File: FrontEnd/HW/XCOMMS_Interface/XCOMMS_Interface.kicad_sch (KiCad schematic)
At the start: 17 parts

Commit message: Altium to KiCad translation of interface board
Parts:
- removed C?: Cap Semi, 0805 SMD Capacitor, symbol COMMS2-altium-import:1_Cap Semi
- removed C? (x4): Cap Semi, 0603 SMD Capacitor, symbol COMMS2-altium-import:3_Cap Semi
- removed C?: Cap Semi, 0603 SMD Capacitor, symbol COMMS2-altium-import:1_Cap Semi
- removed R?: Res3, 0603 SMD Resistor, symbol COMMS2-altium-import:0_Res3
- removed SCRW? (x4): Metric Screw Hole, M3 ScrewHole, symbol COMMS2-altium-import:0_ScrewHole
- removed U?: STM32L4, QFN-33N, symbol COMMS2-altium-import:0_STM32L431Kx
- removed Y?: TCXO 10 MHz, ECS-TXO-2016, symbol COMMS2-altium-import:0_ECS-TXO-2016
- added C1: 4.7uF, Capacitor_SMD:C_0805_2012Metric, symbol Device:C
- added C2, C5: 1uF, Capacitor_SMD:C_0603_1608Metric, symbol Device:C
- added C3, C4, C6: 100nF, Capacitor_SMD:C_0603_1608Metric, symbol Device:C
- added R1: 510, Resistor_SMD:R_0603_1608Metric, symbol Device:R
- added SCRW1, SCRW2, SCRW3, SCRW4: MountingHole_Pad, MountingHole:MountingHole_3.2mm_M3_Pad_Via, symbol Mechanical:MountingHole_Pad
- added U1: STM32L431KBUx, Package_DFN_QFN:QFN-32-1EP_5x5mm_P0.5mm_EP3.45x3.45mm, symbol MCU_ST_STM32L4:STM32L431KBUx
- added Y1: TCXO_ECS, GGS_Miscellaneous:TCXO_ECS, symbol GGS_Miscellaneous:TCXO_ECS
- 12V1: renamed from 12 V?; footprint 532610271 -> Connector_Molex:Molex_PicoBlade_53261-0271_1x02-1MP_P1.25mm_Horizontal; symbol COMMS2-altium-import:0_MOLEX_532610271 -> GGS_Connectors:Picoblade_2x1_H
- JTAG1: renamed from JTAG?; value 532610471 -> MOLEX_532610471; footprint 532610471 -> Connector_Molex:Molex_PicoBlade_53261-0471_1x04-1MP_P1.25mm_Horizontal; symbol COMMS2-altium-import:0_MOLEX_532610471 -> GGS_Connectors:Picoblade_4x1_H
- UART1: renamed from UART?; value 532610471 -> MOLEX_532610471; footprint 532610471 -> Connector_Molex:Molex_PicoBlade_53261-0471_1x04-1MP_P1.25mm_Horizontal; symbol COMMS2-altium-import:0_MOLEX_532610471 -> GGS_Connectors:Picoblade_4x1_H
- gave numbers to parts that had none: 1
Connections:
- net 3V3: now also J1.02; no longer J1.2
- net 5V: now also J1.01; no longer J1.1
- net 5V_EN: now also U1.15 (PB1)
- net 6V_EN: now also U1.14 (PB0)
- net CurrentSense: now also U1.8 (PA2)
- net GND: now also 12V1.MP (MH2), J1.06, J1.08, JTAG1.MP (MH2), UART1.MP (MH2), C1.2, C2.2, C3.2, C4.2, C5.2, C6.2, R1.2, SCRW1.1, SCRW2.1, SCRW3.1, SCRW4.1, U1.16 (VSS), U1.32 (VSS), U1.33 (VSS), Y1.2 (GND); no longer 12V1.0 (MH2), J1.6, J1.8, JTAG1.0 (MH2), UART1.0 (MH2)
- net JTCK: now also U1.24 (PA14)
- net JTDI: now also U1.25 (PA15)
- net JTDO: now also U1.26 (PB3)
- net JTMS: now also U1.23 (PA13)
- net LO_EN: now also J1.05, U1.10 (PA4); no longer J1.5
- net PLL_CSB: now also U1.28 (PB5)
- net R_CSB: now also U1.29 (PB6)
- net SCK: now also U1.11 (PA5)
- net SDI: now also U1.13 (PA7)
- net SDO: now also U1.12 (PA6)
- net T_CSB: now also J1.07, U1.30 (PB7); no longer J1.7
- net Tx_CE: now also J1.09, U1.27 (PB4); no longer J1.9
- net Tx_PM: now also J1.04, U1.7 (PA1); no longer J1.4
- net USART1_CTS: now also U1.21 (PA11)
- net USART1_Rx: now also U1.20 (PA10)
- net USART1_Tx: now also U1.19 (PA9)
- net Vd_PA: now also J1.03; no longer J1.3
- net mcu_OSC: now also U1.6 (PA0), Y1.3 (Out)
- net 12V renamed +12V
- new net +3V3: C1.1, C2.1, C3.1, C4.1, C5.1, C6.1, U1.1 (VDD), U1.17 (VDD), U1.5 (VDDA), Y1.1 (TriState), Y1.4 (Vdd)
- new net Boot0: R1.1, U1.31 (PH3)
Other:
- sheet XCOMMS_PowerSupply ports: added 12V, 3V3, 5V, 5V_EN, 6V_EN, CurrentSense, R_CSB, SCK, SDI, Vd_PA, Vg_PA1, Vg_PA2, Vg_PA3, gnd; removed none
- note added: "Connectors"
- note added: "MCU"
- note added: "Power Supply"
- note added: "Screws"
- note added: "falta cout"
- note removed: "GND has to be connected to JTAG"
- note removed: "nRST has to be connected with JTAG"
- moved on the sheet: 12V1, J1, JTAG1, UART1

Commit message: XCOMMS_RF and XCOMMS_Interface KiCad design updated
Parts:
- added C_TCXO1: 100nF, Capacitor_SMD:C_0603_1608Metric, symbol Device:C
- J2: renamed from UART1; value MOLEX_532610471 -> UART
- J3: renamed from JTAG1; value MOLEX_532610471 -> JTAG
- J4: renamed from 12V1; value MOLEX_52610271 -> 12V
- R1: value 510 -> 10k
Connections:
- net GND: now also C_TCXO1.2
- net mcu_OSC: now also C_TCXO1.1
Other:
- note removed: "falta cout"
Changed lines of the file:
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@@
-    (effects (font (size 1.27 1.27)) (justify left bottom))
-  )
-  (text "falta cout" (at 86.36 82.55 0)
     (effects (font (size 1.27 1.27)) (justify left bottom))
   )
@@
   (symbol (lib_id "GGS_Connectors:Picoblade_4x1_H") (at 97.79 154.94 0) (unit 1)
     (in_bom yes) (on_board yes) (fields_autoplaced)
-    (property "Reference" "JTAG1" (id 0) (at 96.52 134.62 0))
-    (property "Value" "MOLEX_532610471" (id 1) (at 96.52 137.16 0))
+    (property "Reference" "J3" (id 0) (at 96.52 134.62 0))
+    (property "Value" "JTAG" (id 1) (at 96.52 137.16 0))
     (property "Footprint" "Connector_Molex:Molex_PicoBlade_53261-0471_1x04-1MP_P1.25mm_Horizontal" (id 2) (at 97.79 154.94 0)
       (effects (font (size 1.27 1.27)) hide)
@@
     )
     (pin "1")
+  )
+  (symbol (lib_id "Device:C") (at 88.9 82.55 0) (unit 1)
+    (in_bom yes) (on_board yes) (fields_autoplaced)
+    (property "Reference" "C_TCXO1" (id 0) (at 92.71 81.2799 0)
+      (effects (font (size 1.27 1.27)) (justify left))
+    )
+    (property "Value" "100nF" (id 1) (at 92.71 83.8199 0)
+      (effects (font (size 1.27 1.27)) (justify left))
+    )
+    (property "Footprint" "Capacitor_SMD:C_0603_1608Metric" (id 2) (at 89.8652 86.36 0)
+      (effects (font (size 1.27 1.27)) hide)
+    )
+    (property "Datasheet" "~" (id 3) (at 88.9 82.55 0)
+      (effects (font (size 1.27 1.27)) hide)
+    )
+    (pin "1")
+    (pin "2")
   )
   (symbol (lib_id "MCU_ST_STM32L4:STM32L431KBUx") (at 124.46 68.58 0) (unit 1)
@@
   (symbol (lib_id "GGS_Connectors:Picoblade_2x1_H") (at 132.08 154.94 0) (unit 1)
     (in_bom yes) (on_board yes) (fields_autoplaced)
-    (property "Reference" "12V1" (id 0) (at 132.08 139.7 0))
-    (property "Value" "MOLEX_52610271" (id 1) (at 132.08 142.24 0))
+    (property "Reference" "J4" (id 0) (at 132.08 139.7 0))
+    (property "Value" "12V" (id 1) (at 132.08 142.24 0))
     (property "Footprint" "Connector_Molex:Molex_PicoBlade_53261-0271_1x02-1MP_P1.25mm_Horizontal" (id 2) (at 132.08 154.94 0)
       (effects (font (size 1.27 1.27)) hide)
@@
     (pin "1")
   )
+  (symbol (lib_id "power:GND") (at 88.9 86.36 0) (unit 1)
+    (in_bom yes) (on_board yes) (fields_autoplaced)
+    (property "Reference" "#PWR0101" (id 0) (at 88.9 92.71 0)
+      (effects (font (size 1.27 1.27)) hide)
+    )
+    (property "Value" "GND" (id 1) (at 88.9 91.44 0))
+    (property "Footprint" "" (id 2) (at 88.9 86.36 0)
+      (effects (font (size 1.27 1.27)) hide)
+    )
+    (property "Datasheet" "" (id 3) (at 88.9 86.36 0)
+      (effects (font (size 1.27 1.27)) hide)
+    )
+    (pin "1")
+  )
   (symbol (lib_id "power:+3V3") (at 44.5118 71.12 0) (unit 1)
     (in_bom yes) (on_board yes) (fields_autoplaced)
@@
       (effects (font (size 1.27 1.27)) (justify left))
     )
-    (property "Value" "510" (id 1) (at 101.6 66.0399 0)
+    (property "Value" "10k" (id 1) (at 101.6 66.0399 0)
       (effects (font (size 1.27 1.27)) (justify left))
     )
@@
   (symbol (lib_id "GGS_Connectors:Picoblade_4x1_H") (at 97.79 134.62 0) (unit 1)
     (in_bom yes) (on_board yes) (fields_autoplaced)
-    (property "Reference" "UART1" (id 0) (at 96.52 114.3 0))
-    (property "Value" "MOLEX_532610471" (id 1) (at 96.52 116.84 0))
+    (property "Reference" "J2" (id 0) (at 96.52 114.3 0))
+    (property "Value" "UART" (id 1) (at 96.52 116.84 0))
     (property "Footprint" "Connector_Molex:Molex_PicoBlade_53261-0471_1x04-1MP_P1.25mm_Horizontal" (id 2) (at 97.79 134.62 0)
       (effects (font (size 1.27 1.27)) hide)
@@
       (reference "#PWR072") (unit 1) (value "GND") (footprint "")
     )
-    (path "/7af7be37-6e93-4ed7-bb28-3b6dfcb278ed"
-      (reference "12V1") (unit 1) (value "MOLEX_52610271") (footprint "Connector_Molex:Molex_PicoBlade_53261-0271_1x02-1MP_P1.25mm_Horizontal")
+    (path "/8e8c5498-761b-4fad-8a9e-870d060ec873"
+      (reference "#PWR0101") (unit 1) (value "GND") (footprint "")
     )
     (path "/2f6555cb-8bb3-48ae-8adc-4aebbd8da0ca"
@@
       (reference "C40") (unit 1) (value "0.33uF") (footprint "Capacitor_SMD:C_0603_1608Metric")
     )
+    (path "/657fa770-7c96-4254-95e9-81a8281c58b4"
+      (reference "C_TCXO1") (unit 1) (value "100nF") (footprint "Capacitor_SMD:C_0603_1608Metric")
+    )
     (path "/0c671ed6-a6a6-4798-a2b6-204ff4387a8c"
       (reference "J1") (unit 1) (value "TFC-110-02-F-D-A-P-FR") (footprint "GGS_Connectors:SAMTEC_TFC-110-02-F-D-A-P-FR")
     )
+    (path "/b50c6642-ec2d-4f21-8bcb-af36206e84ce"
+      (reference "J2") (unit 1) (value "UART") (footprint "Connector_Molex:Molex_PicoBlade_53261-0471_1x04-1MP_P1.25mm_Horizontal")
+    )
     (path "/0f9289a9-c07b-4423-9227-e6c4d7d06c30"
-      (reference "JTAG1") (unit 1) (value "MOLEX_532610471") (footprint "Connector_Molex:Molex_PicoBlade_53261-0471_1x04-1MP_P1.25mm_Horizontal")
+      (reference "J3") (unit 1) (value "JTAG") (footprint "Connector_Molex:Molex_PicoBlade_53261-0471_1x04-1MP_P1.25mm_Horizontal")
+    )
+    (path "/7af7be37-6e93-4ed7-bb28-3b6dfcb278ed"
+      (reference "J4") (unit 1) (value "12V") (footprint "Connector_Molex:Molex_PicoBlade_53261-0271_1x02-1MP_P1.25mm_Horizontal")
     )
     (path "/1c391ca7-e610-404c-bdff-cd84da814875/575f37ba-97c6-45e5-8a2e-5226df8b97ca"
@@
     )
     (path "/b0dc419d-1860-444a-995b-e370e75d4f19"
-      (reference "R1") (unit 1) (value "510") (footprint "Resistor_SMD:R_0603_1608Metric")
+      (reference "R1") (unit 1) (value "10k") (footprint "Resistor_SMD:R_0603_1608Metric")
     )
     (path "/1c391ca7-e610-404c-bdff-cd84da814875/40b0f3e7-81f1-464f-ba85-11bb7be3476c"
@@
       (reference "U10") (unit 1) (value "MAX870EUK") (footprint "Package_TO_SOT_SMD:SOT-23-5")
     )
-    (path "/b50c6642-ec2d-4f21-8bcb-af36206e84ce"
-      (reference "UART1") (unit 1) (value "MOLEX_532610471") (footprint "Connector_Molex:Molex_PicoBlade_53261-0471_1x04-1MP_P1.25mm_Horizontal")
-    )
     (path "/0e2e05a9-b1d6-423e-ad08-77f5118bb25b"

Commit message: XCOMMS RF update and PA EvalBoard
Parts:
- SCRW1, SCRW2, SCRW3, SCRW4: footprint MountingHole:MountingHole_3.2mm_M3_Pad_Via -> MountingHole:MountingHole_2.7mm_M2.5_Pad
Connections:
- net USART1_CK is gone; now on net GND: J2.4
- net +12V: now also J4.1; no longer J4.2
- net GND: now also J4.2; no longer J4.1
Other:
- note added: "19-03-2022"
- note added: "To Do: Reduce voltage gate inverters to 1 Add LDO for PA Change Picoblade locations"
- note added: "XCOMMS_Interface_v2"
- moved on the sheet: C1, C2, C3, C4, C5, C6, C_TCXO1, J1, J2, J3, J4, R1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

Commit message: XCOMMS Interface rebuild
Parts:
- removed C_TCXO1: 100nF, Capacitor_SMD:C_0603_1608Metric, symbol Device:C
- removed J2: UART, Connector_Molex:Molex_PicoBlade_53261-0471_1x04-1MP_P1.25mm_Horizontal, symbol GGS_Connectors:Picoblade_4x1_H
- removed J3: JTAG, Connector_Molex:Molex_PicoBlade_53261-0471_1x04-1MP_P1.25mm_Horizontal, symbol GGS_Connectors:Picoblade_4x1_H
- removed J4: 12V, Connector_Molex:Molex_PicoBlade_53261-0271_1x02-1MP_P1.25mm_Horizontal, symbol GGS_Connectors:Picoblade_2x1_H
- removed U1: STM32L431KBUx, Package_DFN_QFN:QFN-32-1EP_5x5mm_P0.5mm_EP3.45x3.45mm, symbol MCU_ST_STM32L4:STM32L431KBUx
- removed Y1: TCXO_ECS, GGS_Miscellaneous:TCXO_ECS, symbol GGS_Miscellaneous:TCXO_ECS
- added Annotation1: Silkscreen_Annotation, GGS_Symbols:Bike, symbol GGS_Symbols:Silkscreen_Annotation
- added Annotation2: Silkscreen_Annotation, GGS_Symbols:GGS, symbol GGS_Symbols:Silkscreen_Annotation
- added Annotation3: Silkscreen_Annotation, GGS_Symbols:NSL, symbol GGS_Symbols:Silkscreen_Annotation
- added Annotation4: Silkscreen_Annotation, GGS_Symbols:Prj, symbol GGS_Symbols:Silkscreen_Annotation
- added Annotation5: Silkscreen_Annotation, GGS_Symbols:Rev, symbol GGS_Symbols:Silkscreen_Annotation
- added Annotation6: Silkscreen_Annotation, GGS_Symbols:UPC, symbol GGS_Symbols:Silkscreen_Annotation
- added C41: 20nF, Capacitor_SMD:C_0603_1608Metric, symbol Device:C
- added D1, D2, D3, D4, D5: SZESD9X3.3ST5G, Diode_SMD:D_SOD-923, symbol Device:D_TVS
- added J2, J3: PicoBlade01x05, Connector_Molex:Molex_PicoBlade_53261-0571_1x05-1MP_P1.25mm_Horizontal, symbol Connector_Generic_MountingPin:Conn_01x05_MountingPin
- added J4: PicoBlade01x02, Connector_Molex:Molex_PicoBlade_53261-0271_1x02-1MP_P1.25mm_Horizontal, symbol Connector_Generic_MountingPin:Conn_01x02_MountingPin
- added R22, R23, R24: 10k, Resistor_SMD:R_0603_1608Metric, symbol Device:R
- added R25, R26, R27, R28, R29: 22R, Resistor_SMD:R_0603_1608Metric, symbol Device:R
- added U1: STM32L051K8Tx, Package_QFP:LQFP-32_7x7mm_P0.8mm, symbol MCU_ST_STM32L0:STM32L051K8Tx
- added Y1: ECS-160-8-36B-CKY-TR3, Oscillator:Oscillator_SMD_ECS_2520MV-xxx-xx-4Pin_2.5x2.0mm, symbol Device:Crystal_GND24
- C1: footprint Capacitor_SMD:C_0805_2012Metric -> Capacitor_SMD:C_0603_1608Metric
- C5: value 1uF -> 100nF
- C6: value 100nF -> 20nF
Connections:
- net 3V3 is gone; now on net Vd_PA: J1.02
- net LO_EN is gone; now on net Vg_PA2: J1.05
- net +12V: now also J3.1 (Pin_1), J4.1 (Pin_1)
- net +3V3: now also J1.12, J2.1 (Pin_1), R22.1, R23.1, R24.1, U1.1 (VDD), U1.17 (VDD), U1.5 (VDDA); no longer C5.1, C6.1
- net 5V_EN: now also U1.15 (PB1)
- net 6V_EN: now also U1.14 (PB0)
- net GND: now also J1.09, J1.15, J1.17, J1.19, C41.2, D1.1 (A1), D2.1 (A1), D3.1 (A1), D4.1 (A1), D5.1 (A1), J2.2 (Pin_2), J2.MP (MountPin), J3.4 (Pin_4), J3.5 (Pin_5), J3.MP (MountPin), J4.2 (Pin_2), J4.MP (MountPin), U1.16 (VSS), U1.32 (VSS), Y1.2, Y1.4; no longer J1.08, J1.10, J1.12
- net PLL_CSB: now also U1.28 (PB5)
- net R_CSB: now also U1.9 (PA3)
- net SCK: now also J1.16, U1.11 (PA5); no longer J1.15
- net SDI: now also J1.20, U1.13 (PA7); no longer J1.19
- net SDO: now also J1.18, U1.12 (PA6); no longer J1.17
- net T_CSB: now also J1.08, U1.22 (PA12); no longer J1.07
- net Tx_CE: now also U1.27 (PB4); no longer J1.09
- net Vd_PA: no longer J1.03
- net Vg_PA1: now also J1.07; no longer J1.20
- net Vg_PA2: no longer J1.18
- net Vg_PA3: now also J1.03; no longer J1.16
- net 5V renamed Pout_PA
- net Pout_PA: now also U1.7 (PA1)
- net Boot0 renamed BOOT0
- net BOOT0: now also U1.31 (BOOT0)
- net Tx_PM renamed +5V
- new net: J2.3 (Pin_3), R25.2
- new net: J2.5 (Pin_5), R27.2
- new net: J3.2 (Pin_2), R28.2
- new net: J2.4 (Pin_4), R26.2
- new net: J3.3 (Pin_3), R29.2
- new net I2C1_SCL: D4.2 (A2), R24.2, R28.1, U1.29 (PB6)
- new net I2C1_SDA: D5.2 (A2), R23.2, R29.1, U1.30 (PB7)
- new net Id_PA: U1.8 (PA2)
- new net NRST: C5.1, D3.2 (A2), R22.2, R27.1, U1.4 (NRST)
- new net PLL_CE: J1.10
- new net RCC_IN: C6.1, U1.2 (PC14), Y1.1
- new net RCC_OUT: C41.1, U1.3 (PC15), Y1.3
- new net SCK/SWCLK: D2.2 (A2), R26.1, U1.24 (PA14)
- new net TMS/SWDIO: D1.2 (A2), R25.1, U1.23 (PA13)
- no-connect marks 0 -> 7
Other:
- sheet XCOMMS_PowerSupply ports: added Id_PA; removed 12V, 3V3, 5V, CurrentSense, gnd
- note added: "Silkscreen Annotations"
- moved on the sheet: C1, C2, C3, C4, J1, SCRW1, SCRW2, SCRW3, SCRW4

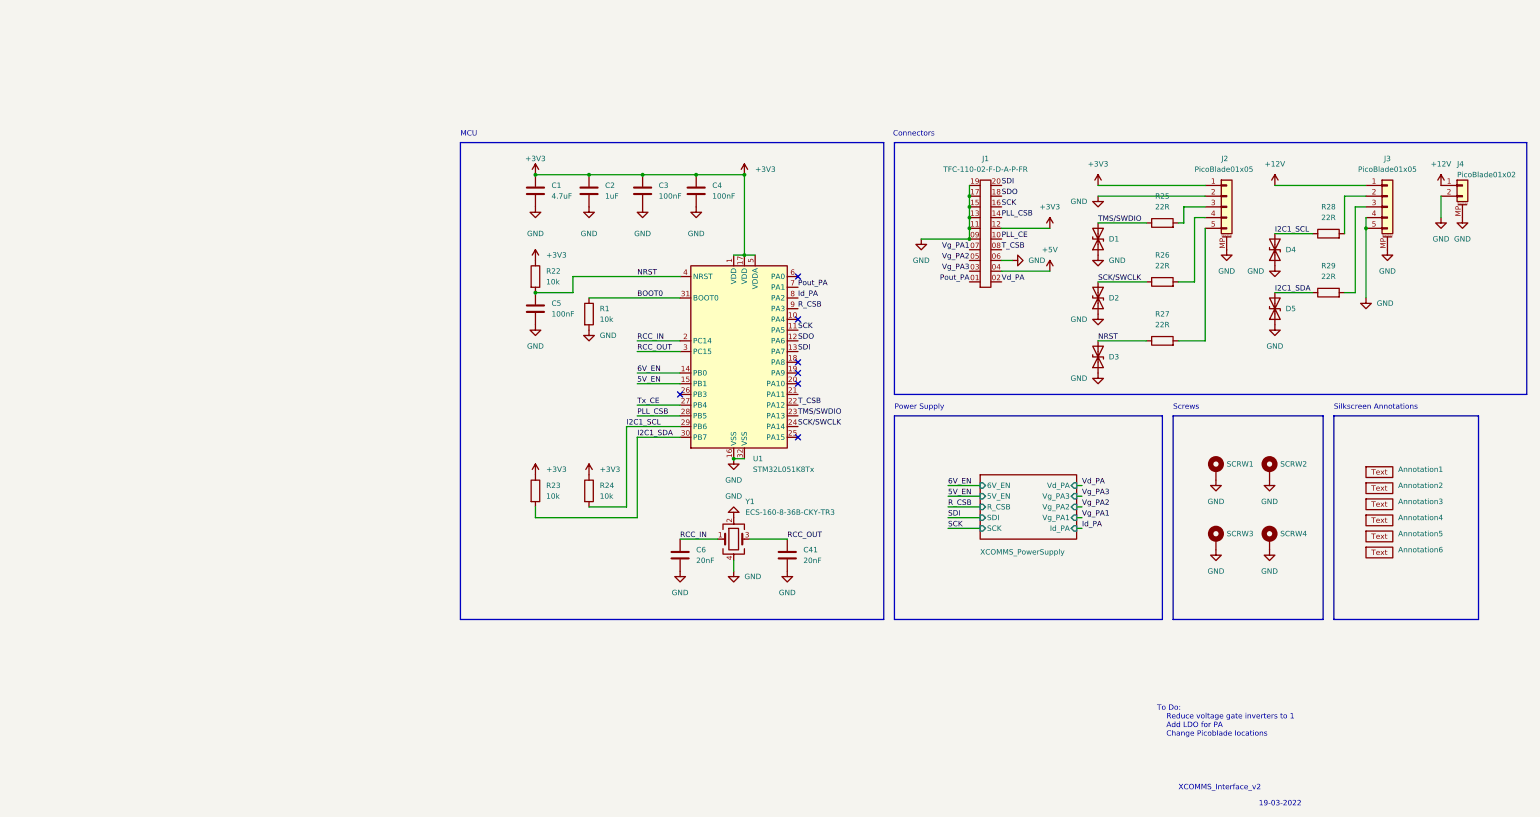
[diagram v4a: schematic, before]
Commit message: xtal changed and routing
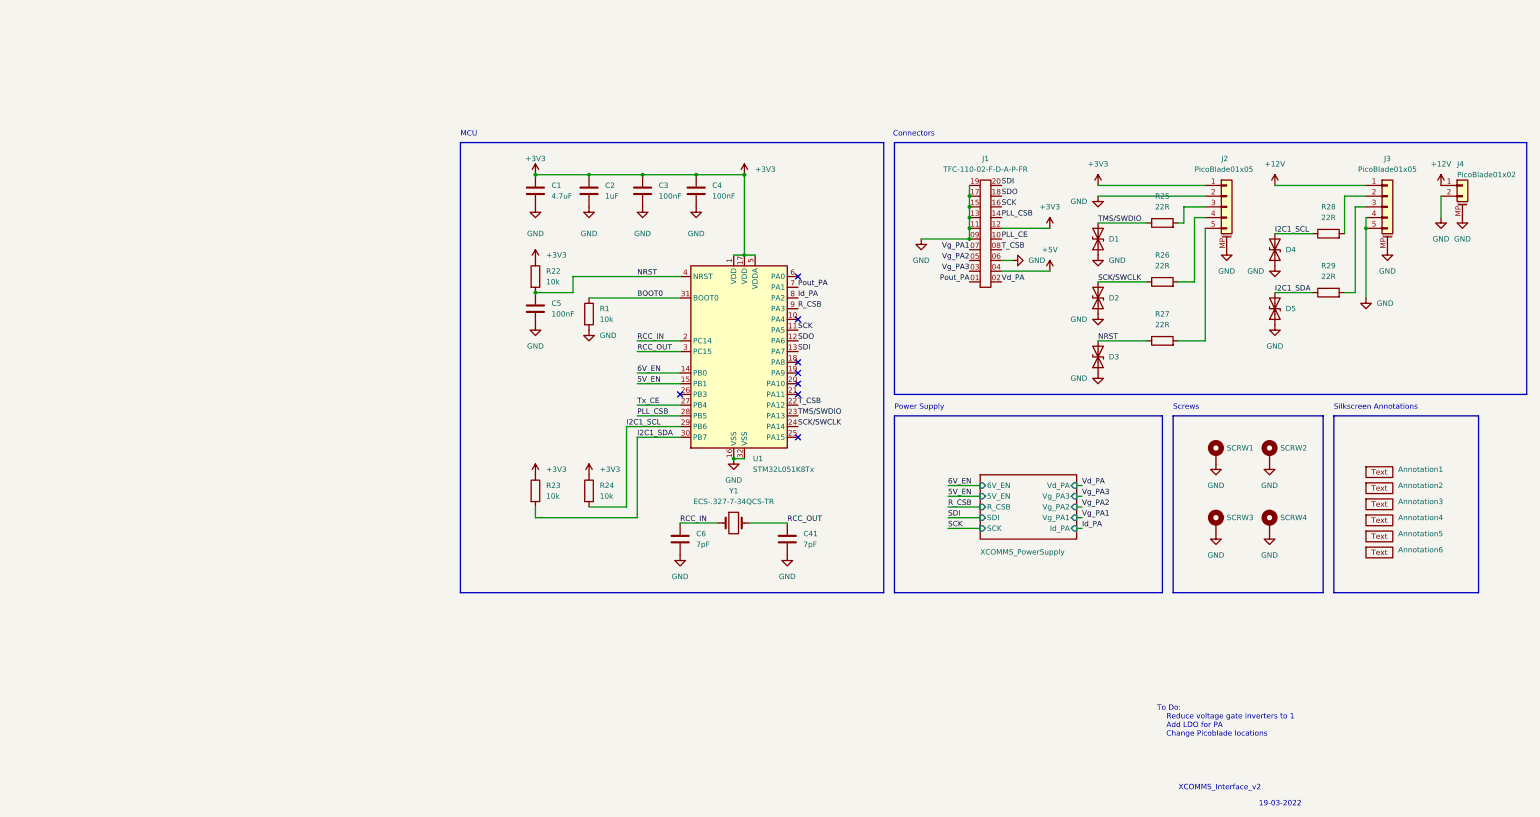
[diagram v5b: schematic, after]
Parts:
- removed Y1: ECS-160-8-36B-CKY-TR3, Oscillator:Oscillator_SMD_ECS_2520MV-xxx-xx-4Pin_2.5x2.0mm, symbol Device:Crystal_GND24
- added Y1: ECS-.327-7-34QCS-TR, Crystal:Crystal_SMD_3215-2Pin_3.2x1.5mm, symbol Device:Crystal
- C41, C6: value 20nF -> 7pF
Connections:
- net RCC_IN: now also Y1.1
- net RCC_OUT: now also Y1.2
- no-connect marks 7 -> 8
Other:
- moved on the sheet: C41, C6, SCRW1, SCRW2, SCRW3, SCRW4
